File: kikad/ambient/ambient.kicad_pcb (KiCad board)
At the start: 2 copper layers, 80 x 66 mm, 69 parts, among them J1 5V DC, J2 FPC 01x10 Female, J3 LED Array, Q1 2N3904, SW2 Next, SW3 Select, SW4 Modify, U1 ATmega328P-PU, U2 AT24C256, U3 AT24C256, U4 AT24C256, U5 AT24C256, Y1 16 MHz

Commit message: minor fixes
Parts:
- Y1: footprint Crystal:Crystal_HC18-U_Vertical -> Crystal:Crystal_HC49-4H_Vertical
- renumbered Reset to SW1
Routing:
- net VCC: track 203.4 -> 162.6 mm

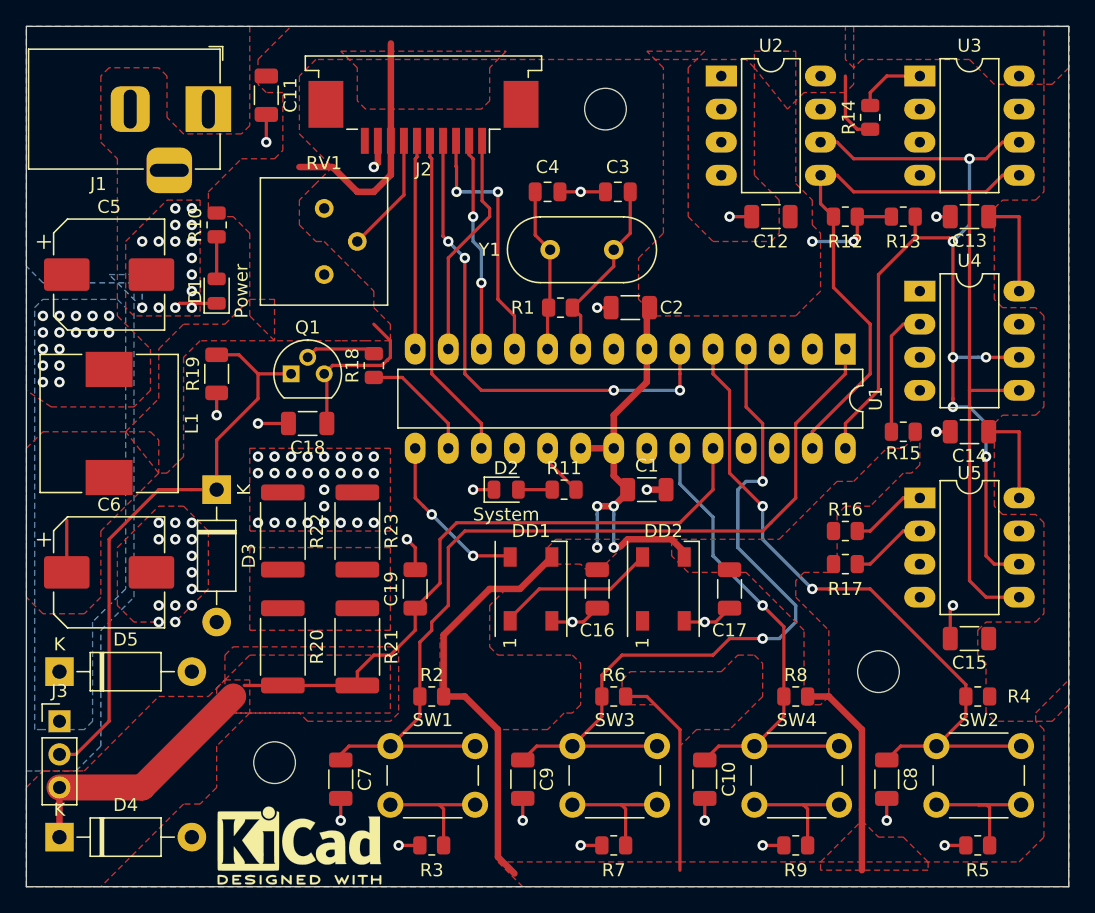
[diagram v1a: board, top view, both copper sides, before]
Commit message: fixes for led ic
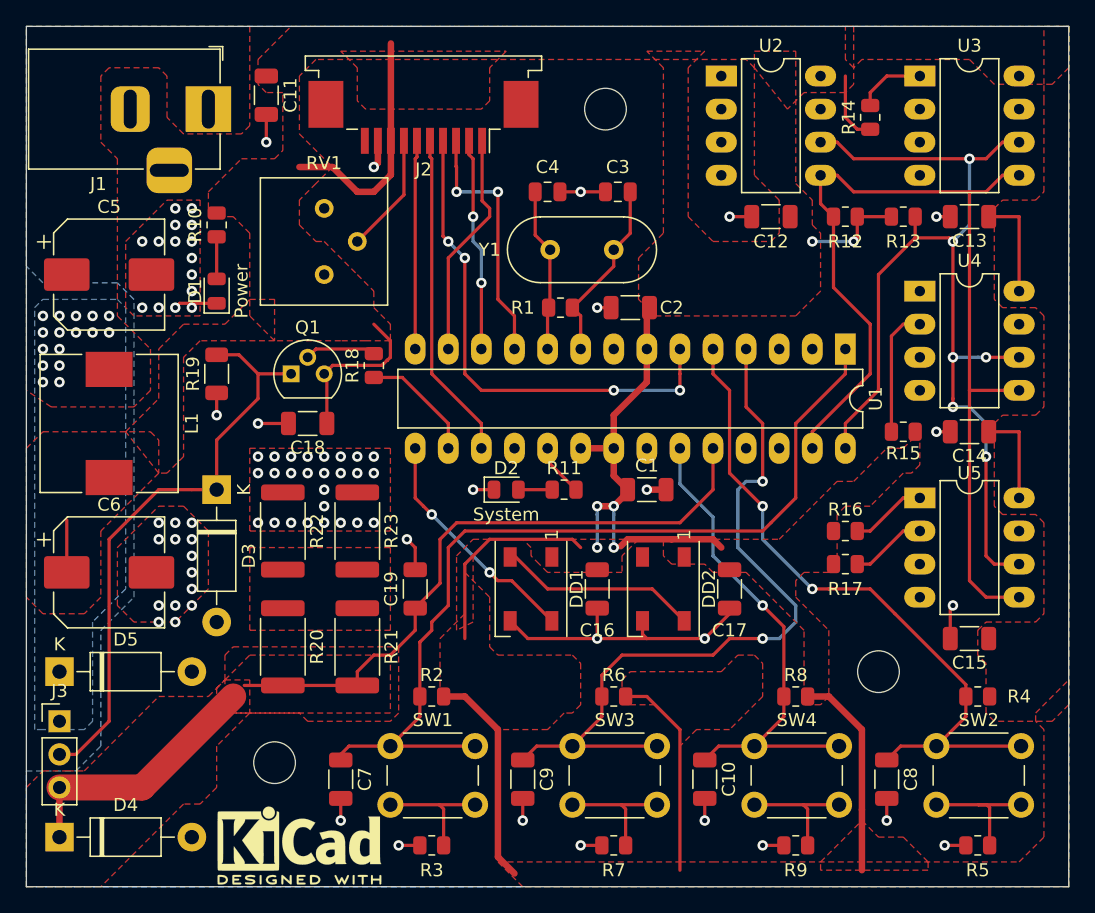
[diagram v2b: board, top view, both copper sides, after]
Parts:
- turned DD1 to 270 degrees
- turned DD2 to 270 degrees
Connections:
- DD1 pad 1: Net-(DD1-Pad1) -> VCC
- DD1 pad 2: GND -> Net-(DD1-Pad2)
- DD1 pad 3: VCC -> GND
- DD2 pad 1: Net-(DD2-Pad1) -> VCC
- DD2 pad 2: GND -> Net-(DD2-Pad2)
- DD2 pad 3: VCC -> GND
- DD2 pad 4: Net-(DD1-Pad1) -> Net-(DD1-Pad2)
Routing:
- net Net-(DD1-Pad2): track 0.00 -> 15.6 mm
- net GND: track 49.8 -> 64.6 mm
- net Net-(DD1-Pad1): track 12.3 -> 0.00 mm
- net PREVIEW_ARRAY: track 13.0 -> 18.3 mm
- net VCC: track 162.6 -> 165.5 mm
